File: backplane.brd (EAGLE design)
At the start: 153.7 x 128.3 mm, 44 parts, among them J1 L717HDE15PD4CH4R, J10 5013310807, J11 5013310807, J12 5013310807, J13 5013310807, J14 5013311007, J15 5013311007, J16 5013311007, J17 5013311007, J18 5013311007, J19 5013311007, J2 1054301102, J20 5013311007, J21 5013311007, J22 5013311007, J23 5013311007, J24 SEAM-40-03.0-S-06-2-A-K-TR, J3 5011902017, J4 5013310807, J5 5013310807, J6 5013310807, J7 5013310807, J8 5013310807, J9 5013310807, U1 AM26LV32EIPWR, U10 AM26LV32EIPWR, U2 AM26LV32EIPWR, U3 AM26LV32EIPWR, U4 AM26LV32EIPWR, U5 AM26LV32EIPWR, U6 AM26LV32EIPWR, U7 AM26LV32EIPWR, U8 AM26LV32EIPWR, U9 AM26LV32EIPWR

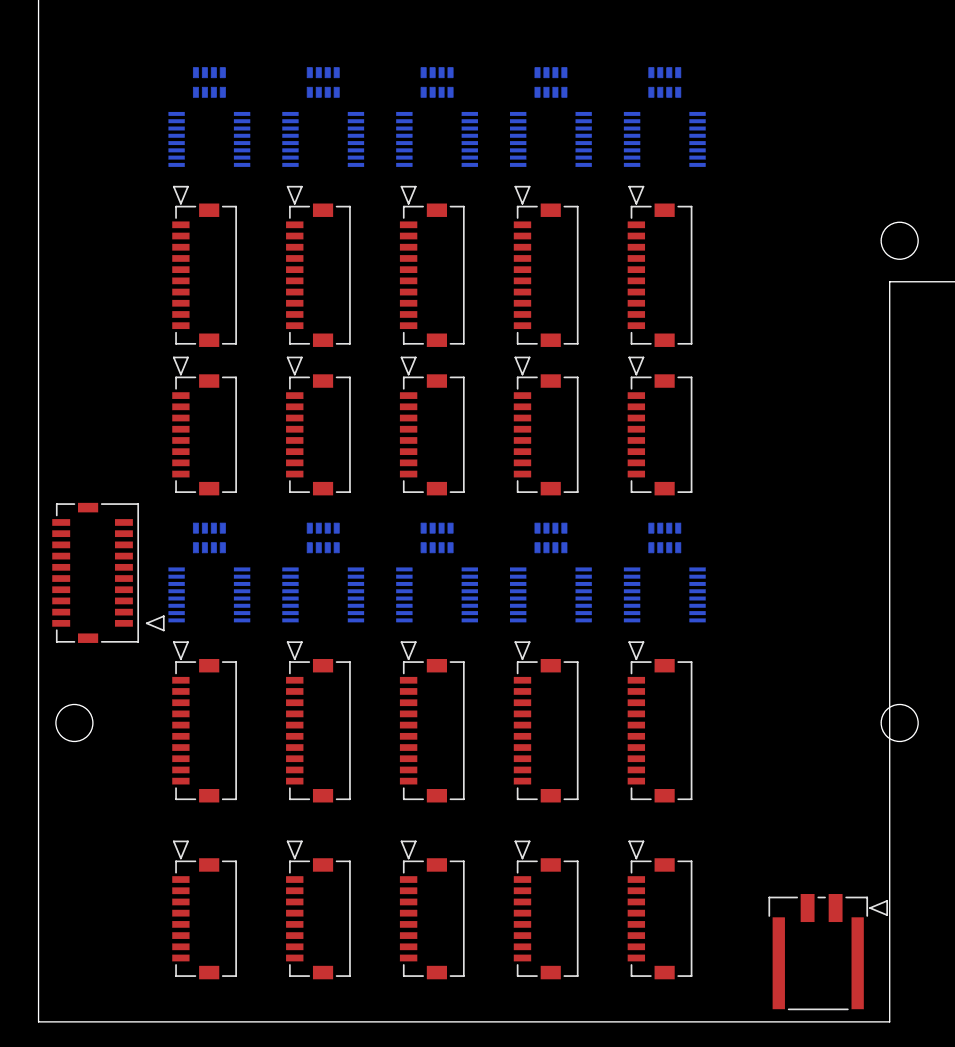
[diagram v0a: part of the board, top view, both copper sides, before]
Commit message: Started routing Encoder/AMC Connectors
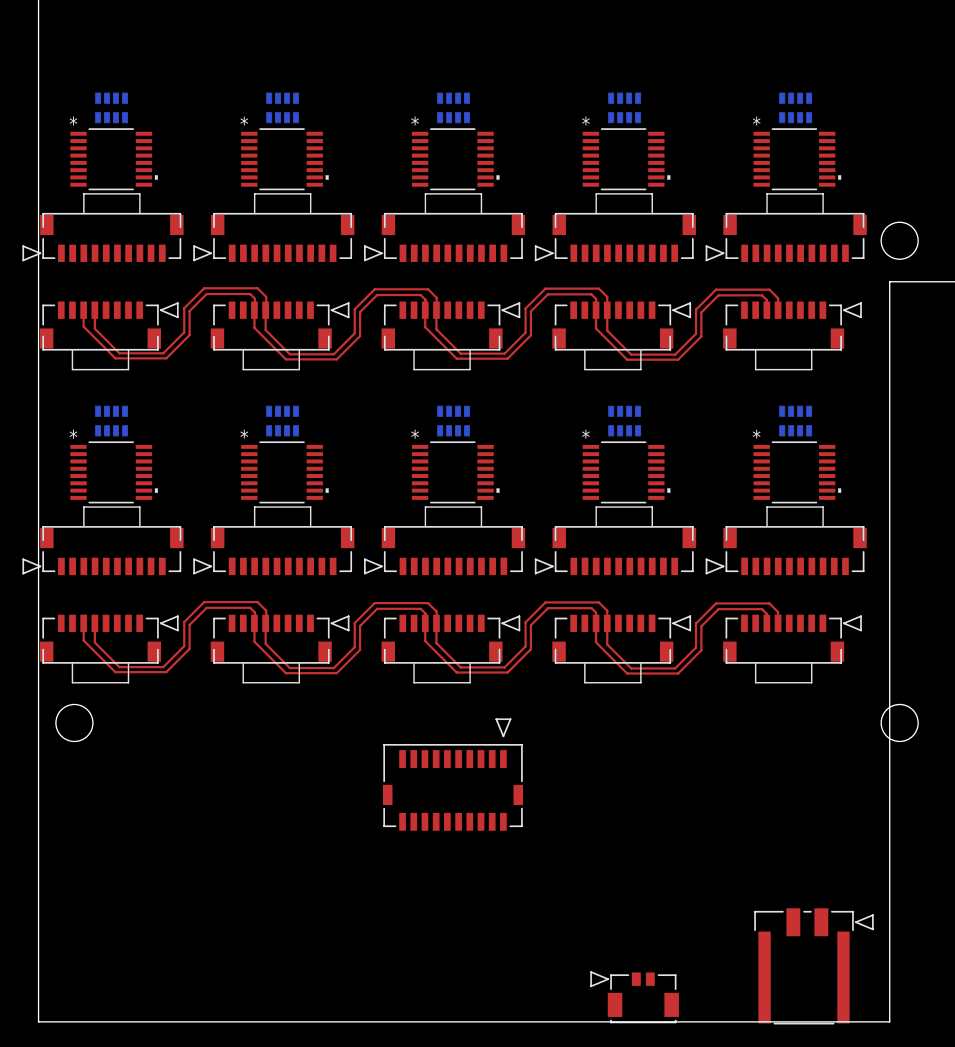
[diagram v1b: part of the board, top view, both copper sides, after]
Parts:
- added J25: 5055670271, sbrio_backplane:CON_5055670271
- moved J3 36.0 mm to (41.5, 23.4), turned to 180 degrees
- moved J13 28.3 mm to (70.0, 35.6), turned to 0 degrees
- moved J12 25.6 mm to (54.7, 35.6), turned to 0 degrees
- moved J11 23.8 mm to (39.5, 35.6), turned to 0 degrees
- moved J9 23.2 mm to (9.03, 35.6), turned to 0 degrees
- moved J10 22.9 mm to (24.3, 35.6), turned to 0 degrees
- moved J8 18.3 mm to (70.0, 63.5), turned to 0 degrees
- moved U10 15.9 mm to (67.4, 49.0), flipped to the top, turned to 0 degrees
- moved RN10 15.7 mm to (67.6, 53.6), turned to 180 degrees
- moved J19 14.7 mm to (2.04, 40.6), turned to 180 degrees
- moved J23 14.0 mm to (63.0, 40.6), turned to 180 degrees
- moved U6 14.0 mm to (6.49, 49.0), flipped to the top, turned to 0 degrees
- moved J7 13.8 mm to (54.7, 63.5), turned to 0 degrees
- moved RN6 13.6 mm to (6.51, 53.6), turned to 180 degrees
- moved U9 12.7 mm to (52.2, 49.0), flipped to the top, turned to 0 degrees
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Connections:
- new net 5V: J14.2, J15.2, J16.2, J17.2, J18.2, J19.2, J20.2, J21.2, J22.2, J23.2
- new net AGND: J10.8, J11.8, J12.8, J13.8, J4.8, J5.8, J6.8, J7.8, J8.8, J9.8
- new net ANA1: J13.7
- new net ANA10: J4.7
- new net ANA2: J8.7
- new net ANA3: J12.7
- new net ANA4: J7.7
- new net ANA5: J11.7
- new net ANA6: J6.7
- new net ANA7: J10.7
- new net ANA8: J5.7
- new net ANA9: J9.7
- new net A_M10_N: J14.9
- new net A_M10_P: J14.10
- new net A_M1_N: J23.9
- new net A_M1_P: J23.10
- new net A_M2_N: J18.9
- new net A_M2_P: J18.10
- new net A_M3_N: J22.9
- new net A_M3_P: J22.10
- new net A_M4_N: J17.9
- new net A_M4_P: J17.10
- new net A_M5_N: J21.9
- new net A_M5_P: J21.10
- new net A_M6_N: J16.9
- new net A_M6_P: J16.10
- new net A_M7_N: J20.9
- new net A_M7_P: J20.10
- new net A_M8_N: J15.9
- new net A_M8_P: J15.10
- new net A_M9_N: J19.9
- new net A_M9_P: J19.10
- new net B_M10_N: J14.7
- new net B_M10_P: J14.8
- new net B_M1_N: J23.7
- new net B_M1_P: J23.8
- new net B_M2_N: J18.7
- new net B_M2_P: J18.8
- new net B_M3_N: J22.7
- new net B_M3_P: J22.8
- new net B_M4_N: J17.7
- new net B_M4_P: J17.8
- new net B_M5_N: J21.7
- new net B_M5_P: J21.8
- new net B_M6_N: J16.7
- new net B_M6_P: J16.8
- new net B_M7_N: J20.7
- new net B_M7_P: J20.8
- new net B_M8_N: J15.7
- new net B_M8_P: J15.8
- new net B_M9_N: J19.7
- new net B_M9_P: J19.8
- new net ESTP+: J10.5, J11.5, J12.5, J13.5, J4.5, J5.5, J6.5, J7.5, J8.5, J9.5
- new net ESTP-: J10.6, J11.6, J12.6, J13.6, J4.6, J5.6, J6.6, J7.6, J8.6, J9.6
- new net MA_M10_N: J14.5, J4.2
- new net MA_M10_P: J14.6, J4.1
- new net MA_M1_N: J13.2, J23.5
- new net MA_M1_P: J13.1, J23.6
- new net MA_M2_N: J18.5, J8.2
- new net MA_M2_P: J18.6, J8.1
- new net MA_M3_N: J12.2, J22.5
- new net MA_M3_P: J12.1, J22.6
- new net MA_M4_N: J17.5, J7.2
- new net MA_M4_P: J17.6, J7.1
- new net MA_M5_N: J11.2, J21.5
- new net MA_M5_P: J11.1, J21.6
- new net MA_M6_N: J16.5, J6.2
- new net MA_M6_P: J16.6, J6.1
- new net MA_M7_N: J10.2, J20.5
- new net MA_M7_P: J10.1, J20.6
- new net MA_M8_N: J15.5, J5.2
- new net MA_M8_P: J15.6, J5.1
- new net MA_M9_N: J19.5, J9.2
- new net MA_M9_P: J19.6, J9.1
- new net SLO_M10_N: J14.3, J4.4
- new net SLO_M10_P: J14.4, J4.3
- new net SLO_M1_N: J13.4, J23.3
- new net SLO_M1_P: J13.3, J23.4
- new net SLO_M2_N: J18.3, J8.4
- new net SLO_M2_P: J18.4, J8.3
- new net SLO_M3_N: J12.4, J22.3
- new net SLO_M3_P: J12.3, J22.4
- new net SLO_M4_N: J17.3, J7.4
- new net SLO_M4_P: J17.4, J7.3
- new net SLO_M5_N: J11.4, J21.3
- new net SLO_M5_P: J11.3, J21.4
- new net SLO_M6_N: J16.3, J6.4
- new net SLO_M6_P: J16.4, J6.3
- new net SLO_M7_N: J10.4, J20.3
- new net SLO_M7_P: J10.3, J20.4
- new net SLO_M8_N: J15.3, J5.4
- new net SLO_M8_P: J15.4, J5.3
- new net SLO_M9_N: J19.3, J9.4
- new net SLO_M9_P: J19.4, J9.3
- net GND: now also J10.10, J10.9, J11.10, J11.9, J12.10, J12.9, J13.10, J13.9, J14.1, J14.11, J14.12, J15.1, J15.11, J15.12, J16.1, J16.11, J16.12, J17.1, J17.11, J17.12, J18.1, J18.11, J18.12, J19.1, J19.11, J19.12, J20.1, J20.11, J20.12, J21.1, J21.11, J21.12, J22.1, J22.11, J22.12, J23.1, J23.11, J23.12, J4.10, J4.9, J5.10, J5.9, J6.10, J6.9, J7.10, J7.9, J8.10, J8.9, J9.10, J9.9
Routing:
- net ESTP+: track 0.00 -> 185.3 mm
- net ESTP-: track 0.00 -> 182.1 mm

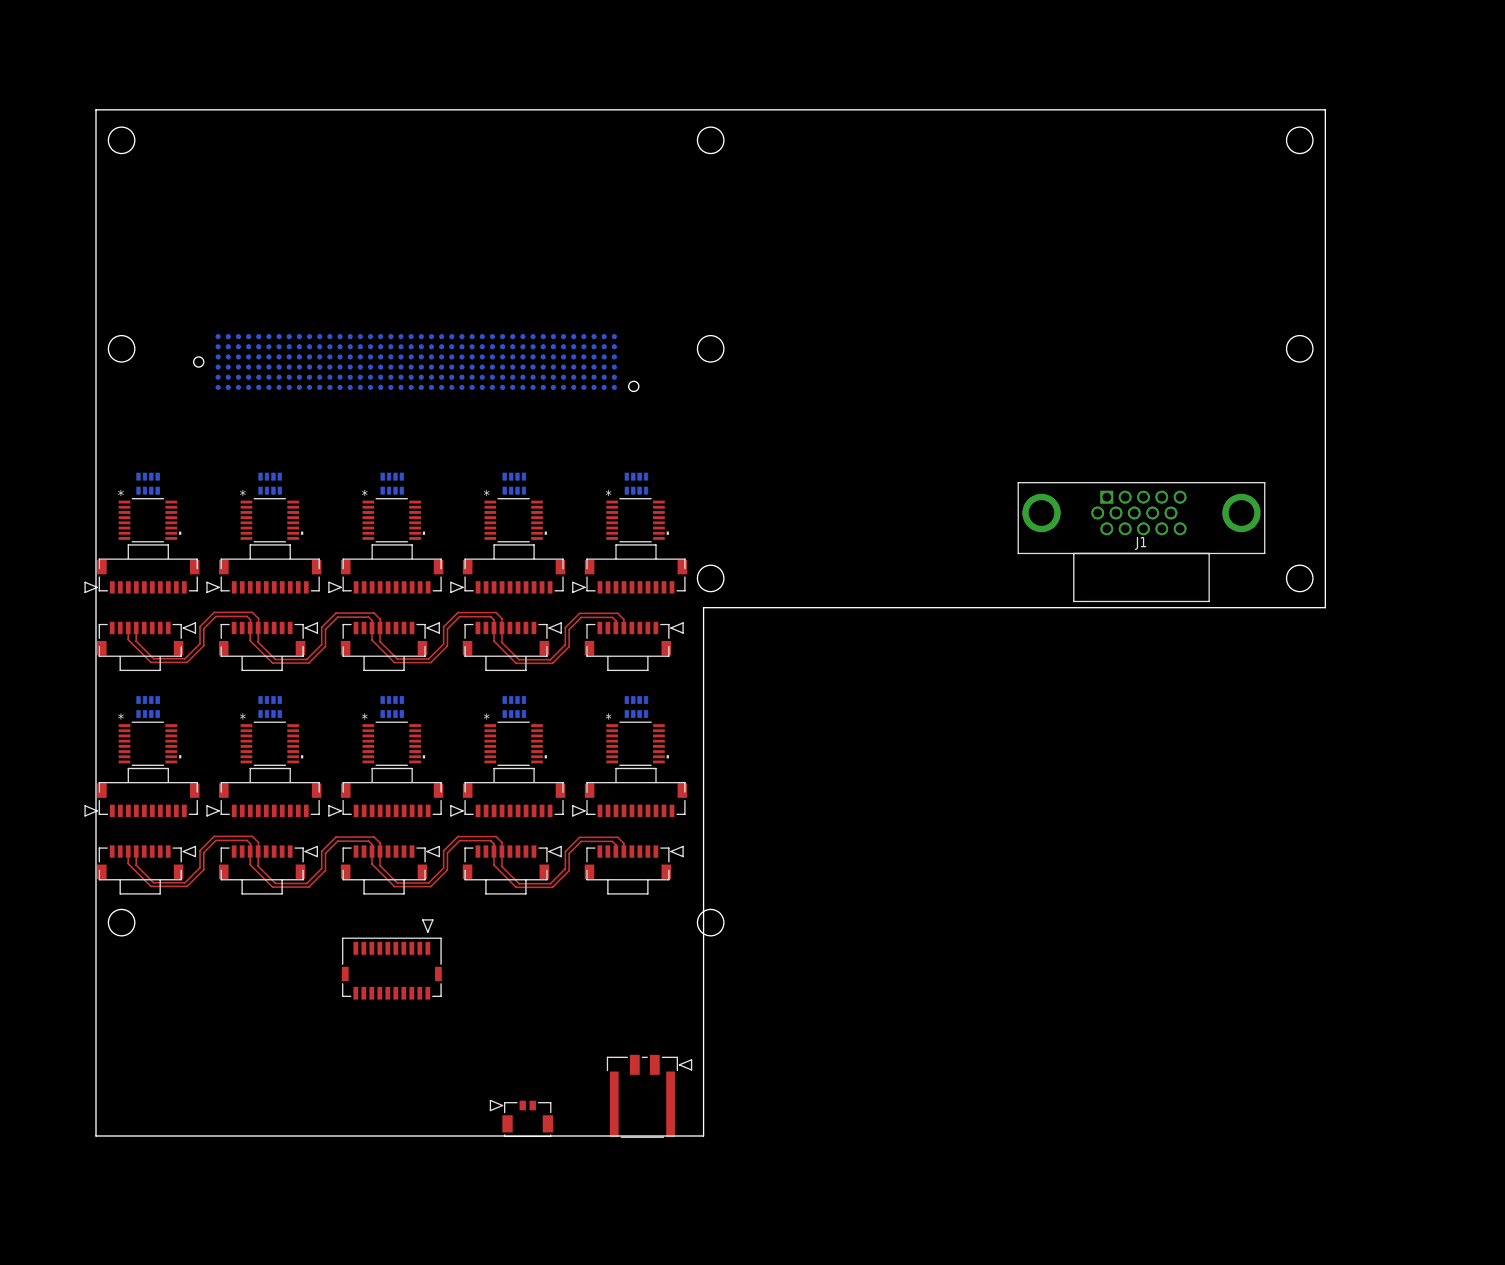
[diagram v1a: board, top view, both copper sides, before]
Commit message: encoder/amc connectors mostly routed
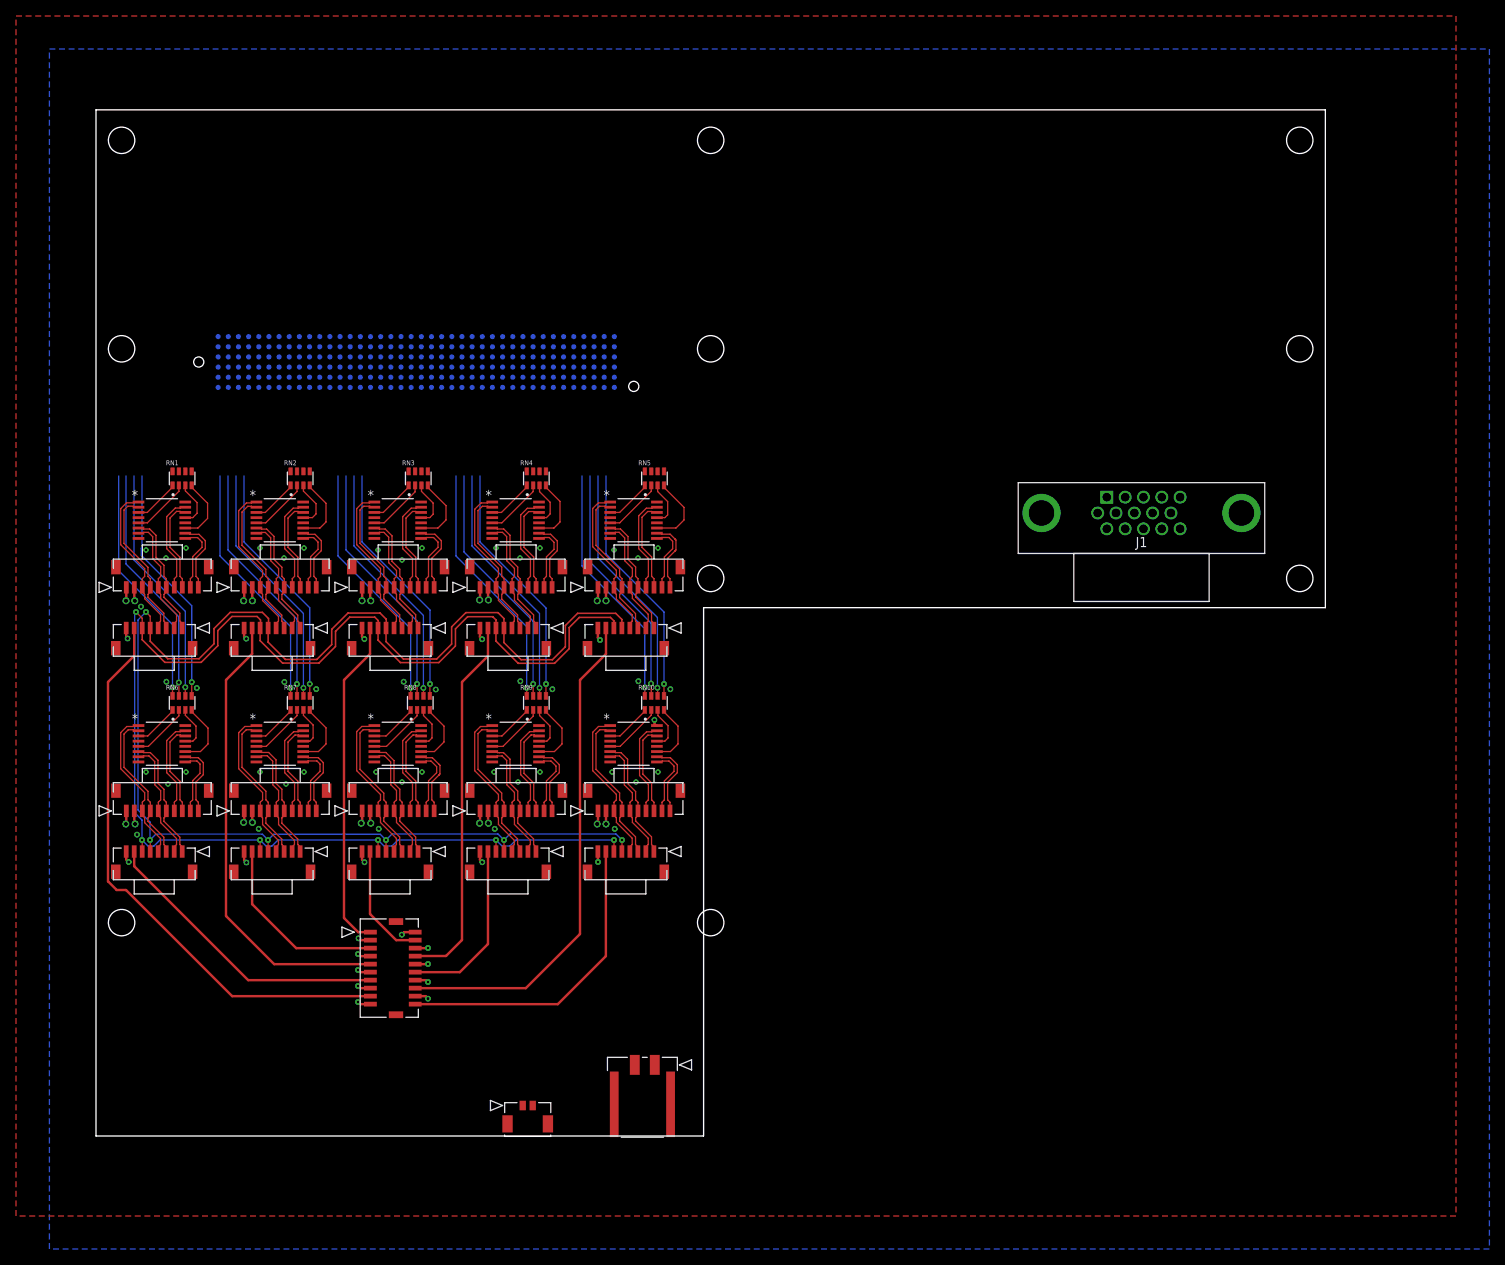
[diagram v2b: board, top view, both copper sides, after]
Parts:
- moved J3 7.46 mm to (34.3, 25.5), turned to 270 degrees
- moved RN1 4.30 mm to (10.8, 82.2), flipped to the top, turned to 0 degrees
- moved RN6 4.28 mm to (10.8, 54.1), flipped to the top, turned to 0 degrees
- moved RN2 3.81 mm to (25.5, 82.2), flipped to the top, turned to 0 degrees
- moved RN7 3.79 mm to (25.5, 54.1), flipped to the top, turned to 0 degrees
- moved RN8 3.54 mm to (40.5, 54.1), flipped to the top, turned to 0 degrees
- moved RN3 3.31 mm to (40.3, 82.2), flipped to the top, turned to 0 degrees
- moved RN4 2.83 mm to (55.0, 82.2), flipped to the top, turned to 0 degrees
- moved RN9 2.80 mm to (55.0, 54.1), flipped to the top, turned to 0 degrees
- moved RN5 2.34 mm to (69.8, 82.2), flipped to the top, turned to 0 degrees
- moved RN10 2.31 mm to (69.8, 54.1), flipped to the top, turned to 0 degrees
- moved J14 1.75 mm to (3.79, 68.6)
- moved J19 1.75 mm to (3.79, 40.6)
- moved J4 1.75 mm to (10.8, 63.5)
- moved J9 1.75 mm to (10.8, 35.6)
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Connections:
- net VCC renamed 3V3
- new net A_M1: RN10.4, U10.11
- new net A_M10: RN1.4, U1.11
- new net A_M2: RN5.4, U5.11
- new net A_M3: RN9.4, U9.11
- new net A_M4: RN4.4, U4.11
- new net A_M5: RN8.4, U8.11
- new net A_M6: RN3.4, U3.11
- new net A_M7: RN7.4, U7.11
- new net A_M8: RN2.4, U2.11
- new net A_M9: RN6.4, U6.11
- new net B_M1: RN10.3, U10.13
- new net B_M10: RN1.3, U1.13
- new net B_M2: RN5.3, U5.13
- new net B_M3: RN9.3, U9.13
- new net B_M4: RN4.3, U4.13
- new net B_M5: RN8.3, U8.13
- new net B_M6: RN3.3, U3.13
- new net B_M7: RN7.3, U7.13
- new net B_M8: RN2.3, U2.13
- new net B_M9: RN6.3, U6.13
- new net MA_M1: RN10.2, U10.5
- new net MA_M10: RN1.2, U1.5
- new net MA_M2: RN5.2, U5.5
- new net MA_M3: RN9.2, U9.5
- new net MA_M4: RN4.2, U4.5
- new net MA_M5: RN8.2, U8.5
- new net MA_M6: RN3.2, U3.5
- new net MA_M7: RN7.2, U7.5
- new net MA_M8: RN2.2, U2.5
- new net MA_M9: RN6.2, U6.5
- new net N$1: RN9.5
- new net N$10: RN10.7
- new net N$108: U4.4
- new net N$11: RN10.8
- new net N$115: U3.12
- new net N$12: RN8.7
- new net N$124: U3.4
- new net N$13: U10.4
- new net N$131: U2.12
- new net N$14: RN8.8
- new net N$140: U2.4
- new net N$147: U1.12
- new net N$15: RN7.5
- new net N$156: U1.4
- new net N$16: RN7.6
- new net N$17: RN7.7
- new net N$18: RN7.8
- new net N$19: RN6.5
- new net N$2: RN9.6
- new net N$20: RN6.6
- new net N$21: RN6.7
- new net N$22: RN6.8
- new net N$23: U9.12
- new net N$24: RN5.5
- new net N$25: RN5.6
- new net N$26: RN5.7
- new net N$27: RN5.8
- new net N$28: RN4.5
- new net N$29: RN4.6
- new net N$3: RN9.7
- new net N$30: U9.4
- new net N$31: RN4.7
- new net N$32: RN4.8
- new net N$33: RN3.5
- new net N$34: RN3.6
- new net N$35: RN3.7
- new net N$36: RN3.8
- new net N$37: U8.12
- new net N$38: RN2.5
- new net N$39: RN2.6
- new net N$4: U10.12
- new net N$40: RN2.7
- new net N$41: RN2.8
- new net N$42: RN1.5
- new net N$43: RN1.6
- new net N$44: U8.4
- new net N$45: RN1.7
- new net N$46: RN1.8
- new net N$5: RN9.8
- new net N$51: U7.12
- new net N$6: RN8.5
- new net N$60: U7.4
- new net N$67: U6.12
- new net N$7: RN8.6
- new net N$76: U6.4
- new net N$8: RN10.5
- new net N$85: U5.12
- new net N$9: RN10.6
- new net N$92: U5.4
- new net N$99: U4.12
- new net SLO_M1: RN10.1, U10.3
- new net SLO_M10: RN1.1, U1.3
- new net SLO_M2: RN5.1, U5.3
- new net SLO_M3: RN9.1, U9.3
- new net SLO_M4: RN4.1, U4.3
- new net SLO_M5: RN8.1, U8.3
- new net SLO_M6: RN3.1, U3.3
- new net SLO_M7: RN7.1, U7.3
- new net SLO_M8: RN2.1, U2.3
- new net SLO_M9: RN6.1, U6.3
- net AGND: now also J3.10, J3.11, J3.14, J3.15, J3.18, J3.19, J3.2, J3.3, J3.6, J3.7
- net ANA1: now also J3.20
- net ANA10: now also J3.17
- net ANA2: now also J3.16
- net ANA3: now also J3.12
- net ANA4: now also J3.8
- net ANA5: now also J3.4
- net ANA6: now also J3.1
- net ANA7: now also J3.5
- net ANA8: now also J3.9
- net ANA9: now also J3.13
- net A_M10_N: now also U1.9
- net A_M10_P: now also U1.10
- net A_M1_N: now also U10.9
- net A_M1_P: now also U10.10
- net A_M2_N: now also U5.9
- net A_M2_P: now also U5.10
- net A_M3_N: now also U9.9
- net A_M3_P: now also U9.10
- net A_M4_N: now also U4.9
- net A_M4_P: now also U4.10
- net A_M5_N: now also U8.9
- net A_M5_P: now also U8.10
- net A_M6_N: now also U3.9
- net A_M6_P: now also U3.10
- net A_M7_N: now also U7.9
- net A_M7_P: now also U7.10
- net A_M8_N: now also U2.9
- net A_M8_P: now also U2.10
- net A_M9_N: now also U6.9
- net A_M9_P: now also U6.10
- net B_M10_N: now also U1.15
- net B_M10_P: now also U1.14
- net B_M1_N: now also U10.15
- net B_M1_P: now also U10.14
- net B_M2_N: now also U5.15
- net B_M2_P: now also U5.14
- net B_M3_N: now also U9.15
- net B_M3_P: now also U9.14
- net B_M4_N: now also U4.15
- net B_M4_P: now also U4.14
- net B_M5_N: now also U8.15
- net B_M5_P: now also U8.14
- net B_M6_N: now also U3.15
- net B_M6_P: now also U3.14
- net B_M7_N: now also U7.15
- net B_M7_P: now also U7.14
- net B_M8_N: now also U2.15
- net B_M8_P: now also U2.14
- net B_M9_N: now also U6.15
- net B_M9_P: now also U6.14
- net GND: now also J3.21, J3.22
- net MA_M10_N: now also U1.7
- net MA_M10_P: now also U1.6
- net MA_M1_N: now also U10.7
- net MA_M1_P: now also U10.6
- net MA_M2_N: now also U5.7
- net MA_M2_P: now also U5.6
- net MA_M3_N: now also U9.7
- net MA_M3_P: now also U9.6
- net MA_M4_N: now also U4.7
- net MA_M4_P: now also U4.6
- net MA_M5_N: now also U8.7
- net MA_M5_P: now also U8.6
- net MA_M6_N: now also U3.7
- net MA_M6_P: now also U3.6
- net MA_M7_N: now also U7.7
- net MA_M7_P: now also U7.6
- net MA_M8_N: now also U2.7
- net MA_M8_P: now also U2.6
- net MA_M9_N: now also U6.7
- net MA_M9_P: now also U6.6
- net SLO_M10_N: now also U1.1
- net SLO_M10_P: now also U1.2
- net SLO_M1_N: now also U10.1
- net SLO_M1_P: now also U10.2
- net SLO_M2_N: now also U5.1
- net SLO_M2_P: now also U5.2
- net SLO_M3_N: now also U9.1
- net SLO_M3_P: now also U9.2
- net SLO_M4_N: now also U4.1
- net SLO_M4_P: now also U4.2
- net SLO_M5_N: now also U8.1
- net SLO_M5_P: now also U8.2
- net SLO_M6_N: now also U3.1
- net SLO_M6_P: now also U3.2
- net SLO_M7_N: now also U7.1
- net SLO_M7_P: now also U7.2
- net SLO_M8_N: now also U2.1
- net SLO_M8_P: now also U2.2
- net SLO_M9_N: now also U6.1
- net SLO_M9_P: now also U6.2
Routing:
- net AGND: track 0.00 -> 427.2 mm, vias 0 -> 20
- net ANA10: track 0.00 -> 71.8 mm
- net ANA2: track 0.00 -> 63.0 mm
- net ANA8: track 0.00 -> 57.9 mm
- net ANA4: track 0.00 -> 47.0 mm
- net ANA6: track 0.00 -> 41.6 mm
- net ANA1: track 0.00 -> 39.4 mm
- net ANA9: track 0.00 -> 37.3 mm
- net N$14: track 0.00 -> 31.2 mm, vias 0 -> 1
- net N$12: track 0.00 -> 31.2 mm, vias 0 -> 1
- net N$5: track 0.00 -> 31.1 mm, vias 0 -> 1
- net N$18: track 0.00 -> 31.1 mm, vias 0 -> 1
- net N$7: track 0.00 -> 31.1 mm, vias 0 -> 1
- net N$3: track 0.00 -> 31.1 mm, vias 0 -> 1
- net N$17: track 0.00 -> 31.1 mm, vias 0 -> 1
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- added copper zone on layer 15, net 5V
- added copper zone on layer 1, net GND
- added copper zone on layer 16, net GND
- added copper zone on layer 2, net GND
